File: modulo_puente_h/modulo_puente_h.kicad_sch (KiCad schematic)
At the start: 15 parts, among them M1 Motor_IZQ, M2 Motor_DER, U1 L298N

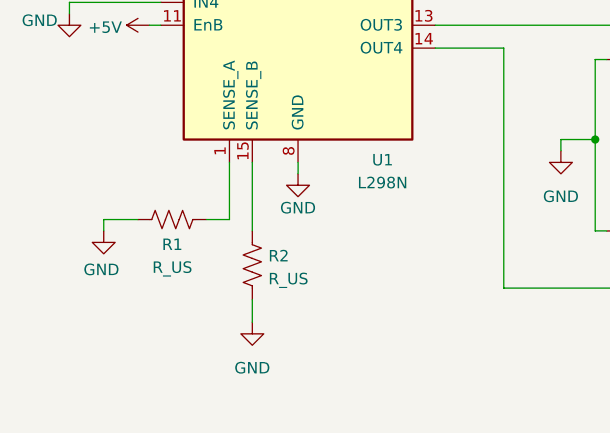
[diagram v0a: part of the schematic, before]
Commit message: fix(puente-h): Las salidas de sensor no tenian PWR_FLAG
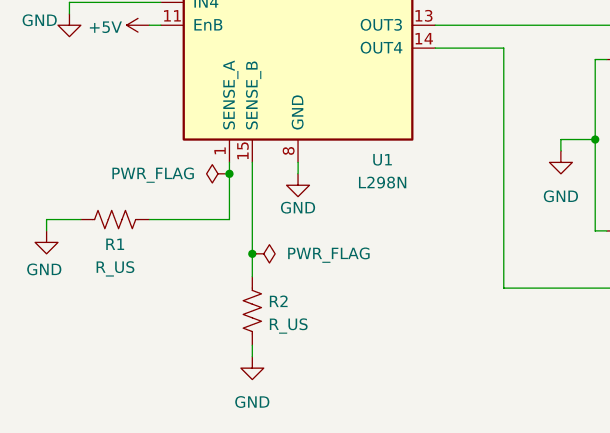
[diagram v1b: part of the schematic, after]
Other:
- moved on the sheet: R1, R2
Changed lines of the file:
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@@
 	)
 	(junction
+		(at 86.36 109.22)
+		(diameter 0)
+		(color 0 0 0 0)
+	)
+	(junction
 		(at 96.52 63.5)
 		(diameter 0)
@@
 	)
 	(junction
+		(at 88.9 118.11)
+		(diameter 0)
+		(color 0 0 0 0)
+	)
+	(junction
 		(at 127 71.12)
 		(diameter 0)
@@
 	(wire
 		(pts
-			(xy 86.36 107.95) (xy 86.36 114.3)
+			(xy 86.36 107.95) (xy 86.36 109.22)
 		)
 		(stroke
@@
 	(wire
 		(pts
-			(xy 86.36 114.3) (xy 83.82 114.3)
+			(xy 86.36 114.3) (xy 77.47 114.3)
 		)
 		(stroke
@@
 	(wire
 		(pts
-			(xy 88.9 125.73) (xy 88.9 123.19)
+			(xy 88.9 129.54) (xy 88.9 128.27)
 		)
 		(stroke
@@
 	(wire
 		(pts
-			(xy 76.2 114.3) (xy 72.39 114.3)
+			(xy 69.85 114.3) (xy 66.04 114.3)
 		)
 		(stroke
@@
 	(wire
 		(pts
-			(xy 88.9 107.95) (xy 88.9 115.57)
+			(xy 88.9 107.95) (xy 88.9 118.11)
 		)
 		(stroke
@@
 	(wire
 		(pts
+			(xy 86.36 109.22) (xy 86.36 114.3)
+		)
+		(stroke
+			(width 0)
+			(type default)
+		)
+	)
+	(wire
+		(pts
 			(xy 205.74 77.47) (xy 209.55 77.47)
 		)
@@
 	(wire
 		(pts
+			(xy 88.9 118.11) (xy 88.9 120.65)
+		)
+		(stroke
+			(width 0)
+			(type default)
+		)
+	)
+	(wire
+		(pts
 			(xy 149.86 115.57) (xy 151.13 115.57)
 		)
@@
 	(wire
 		(pts
-			(xy 72.39 114.3) (xy 72.39 115.57)
+			(xy 66.04 114.3) (xy 66.04 115.57)
 		)
 		(stroke
@@
 	(symbol
 		(lib_id "power:GNDS")
-		(at 72.39 115.57 0)
+		(at 66.04 115.57 0)
 		(unit 1)
 		(exclude_from_sim no)
@@
 		(dnp no)
 		(property "Reference" "#PWR015"
-			(at 72.39 121.92 0)
+			(at 66.04 121.92 0)
 			(effects
 				(font
@@
 		)
 		(property "Value" "GND"
-			(at 72.136 119.888 0)
+			(at 65.786 119.888 0)
 			(effects
 				(font
@@
 		)
 		(property "Footprint" ""
-			(at 72.39 115.57 0)
+			(at 66.04 115.57 0)
 			(effects
 				(font
@@
 		)
 		(property "Datasheet" ""
-			(at 72.39 115.57 0)
+			(at 66.04 115.57 0)
 			(effects
 				(font
@@
 		)
 		(property "Description" "Power symbol creates a global label with name \"GNDS\" , signal ground"
-			(at 72.39 115.57 0)
+			(at 66.04 115.57 0)
 			(effects
 				(font
@@
 	(symbol
 		(lib_id "power:PWR_FLAG")
+		(at 88.9 118.11 270)
+		(unit 1)
+		(exclude_from_sim no)
+		(in_bom yes)
+		(on_board yes)
+		(dnp no)
+		(fields_autoplaced yes)
+		(property "Reference" "#FLG07"
+			(at 90.805 118.11 0)
+			(effects
+				(font
+					(size 1.27 1.27)
+				)
+				(hide yes)
+			)
+		)
+		(property "Value" "PWR_FLAG"
+			(at 92.71 118.1099 90)
+			(effects
+				(font
+					(size 1.27 1.27)
+				)
+				(justify left)
+			)
+		)
+		(property "Footprint" ""
+			(at 88.9 118.11 0)
+			(effects
+				(font
+					(size 1.27 1.27)
+				)
+				(hide yes)
+			)
+		)
+		(property "Datasheet" "~"
+			(at 88.9 118.11 0)
+			(effects
+				(font
+					(size 1.27 1.27)
+				)
+				(hide yes)
+			)
+		)
+		(property "Description" "Special symbol for telling ERC where power comes from"
+			(at 88.9 118.11 0)
+			(effects
+				(font
+					(size 1.27 1.27)
+				)
+				(hide yes)
+			)
+		)
+		(pin "1"
+		)
+		(instances
+			(project "modulo_puente_h"
+				(path "/e8bedf4c-52de-4280-a6f9-25032b7792a2"
+					(reference "#FLG07")
+					(unit 1)
+				)
+			)
+		)
+	)
+	(symbol
+		(lib_id "power:PWR_FLAG")
 		(at 243.84 97.79 0)
 		(unit 1)
@@
 	(symbol
 		(lib_id "power:GNDS")
-		(at 88.9 125.73 0)
+		(at 88.9 129.54 0)
 		(unit 1)
 		(exclude_from_sim no)
@@
 		(fields_autoplaced yes)
 		(property "Reference" "#PWR016"
-			(at 88.9 132.08 0)
+			(at 88.9 135.89 0)
 			(effects
 				(font
@@
 		)
 		(property "Value" "GND"
-			(at 88.9 130.81 0)
+			(at 88.9 134.62 0)
 			(effects
 				(font
@@
 		)
 		(property "Footprint" ""
-			(at 88.9 125.73 0)
+			(at 88.9 129.54 0)
 			(effects
 				(font
@@
 		)
 		(property "Datasheet" ""
-			(at 88.9 125.73 0)
+			(at 88.9 129.54 0)
 			(effects
 				(font
@@
 		)
 		(property "Description" "Power symbol creates a global label with name \"GNDS\" , signal ground"
-			(at 88.9 125.73 0)
+			(at 88.9 129.54 0)
 			(effects
 				(font
@@
 	(symbol
 		(lib_id "Device:R_US")
-		(at 88.9 119.38 180)
+		(at 88.9 124.46 180)
 		(unit 1)
 		(exclude_from_sim no)
@@
 		(dnp no)
 		(property "Reference" "R2"
-			(at 90.678 118.364 0)
+			(at 90.678 123.444 0)
 			(effects
 				(font
@@
 		)
 		(property "Value" "R_US"
-			(at 90.678 120.904 0)
+			(at 90.678 125.984 0)
 			(effects
 				(font
@@
 		)
 		(property "Footprint" ""
-			(at 87.884 119.126 90)
+			(at 87.884 124.206 90)
 			(effects
 				(font
@@
 		)
 		(property "Datasheet" "~"
-			(at 88.9 119.38 0)
+			(at 88.9 124.46 0)
 			(effects
 				(font
@@
 		)
 		(property "Description" "Resistor, US symbol"
-			(at 88.9 119.38 0)
+			(at 88.9 124.46 0)
 			(effects
 				(font
@@
 	)
 	(symbol
+		(lib_id "power:PWR_FLAG")
+		(at 86.36 109.22 90)
+		(unit 1)
+		(exclude_from_sim no)
+		(in_bom yes)
+		(on_board yes)
+		(dnp no)
+		(fields_autoplaced yes)
+		(property "Reference" "#FLG06"
+			(at 84.455 109.22 0)
+			(effects
+				(font
+					(size 1.27 1.27)
+				)
+				(hide yes)
+			)
+		)
+		(property "Value" "PWR_FLAG"
+			(at 82.55 109.2199 90)
+			(effects
+				(font
+					(size 1.27 1.27)
+				)
+				(justify left)
+			)
+		)
+		(property "Footprint" ""
+			(at 86.36 109.22 0)
+			(effects
+				(font
+					(size 1.27 1.27)
+				)
+				(hide yes)
+			)
+		)
+		(property "Datasheet" "~"
+			(at 86.36 109.22 0)
+			(effects
+				(font
+					(size 1.27 1.27)
+				)
+				(hide yes)
+			)
+		)
+		(property "Description" "Special symbol for telling ERC where power comes from"
+			(at 86.36 109.22 0)
+			(effects
+				(font
+					(size 1.27 1.27)
+				)
+				(hide yes)
+			)
+		)
+		(pin "1"
+		)
+		(instances
+			(project ""
+				(path "/e8bedf4c-52de-4280-a6f9-25032b7792a2"
+					(reference "#FLG06")
+					(unit 1)
+				)
+			)
+		)
+	)
+	(symbol
 		(lib_id "power:GND")
 		(at 123.19 106.68 0)
@@
 	(symbol
 		(lib_id "Device:R_US")
-		(at 80.01 114.3 270)
+		(at 73.66 114.3 270)
 		(unit 1)
 		(exclude_from_sim no)
@@
 		(dnp no)
 		(property "Reference" "R1"
-			(at 80.01 117.094 90)
+			(at 73.66 117.094 90)
 			(effects
 				(font
@@
 		)
 		(property "Value" "R_US"
-			(at 80.01 119.634 90)
+			(at 73.66 119.634 90)
 			(effects
 				(font
@@
 		)
 		(property "Footprint" ""
-			(at 79.756 115.316 90)
+			(at 73.406 115.316 90)
 			(effects
 				(font
@@
 		)
 		(property "Datasheet" "~"
-			(at 80.01 114.3 0)
+			(at 73.66 114.3 0)
 			(effects
 				(font
@@
 		)
 		(property "Description" "Resistor, US symbol"
-			(at 80.01 114.3 0)
+			(at 73.66 114.3 0)
 			(effects
 				(font

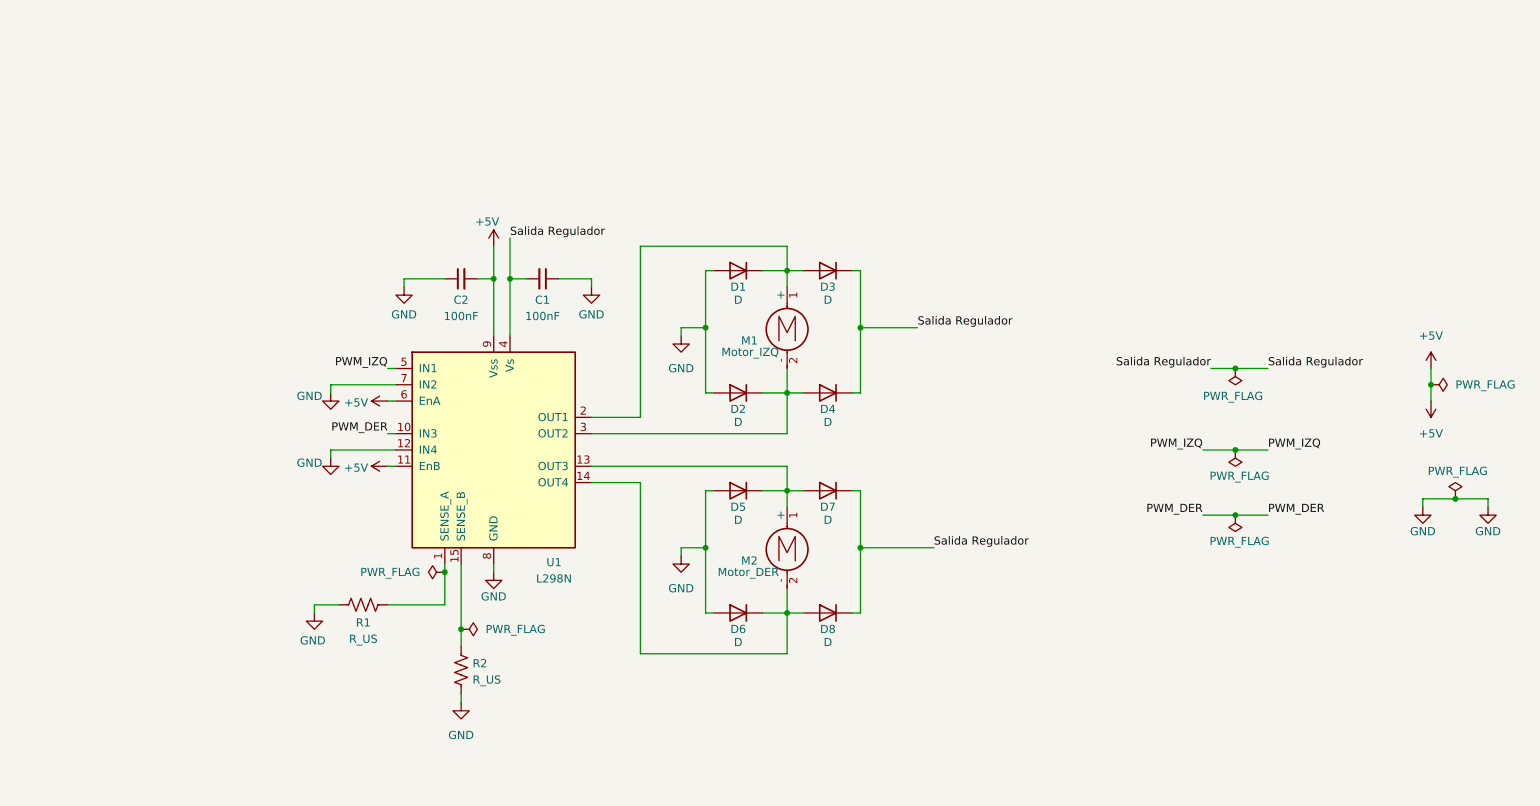
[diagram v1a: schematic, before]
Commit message: refactor(puente-h):Modifico el orden de los pines de conexión
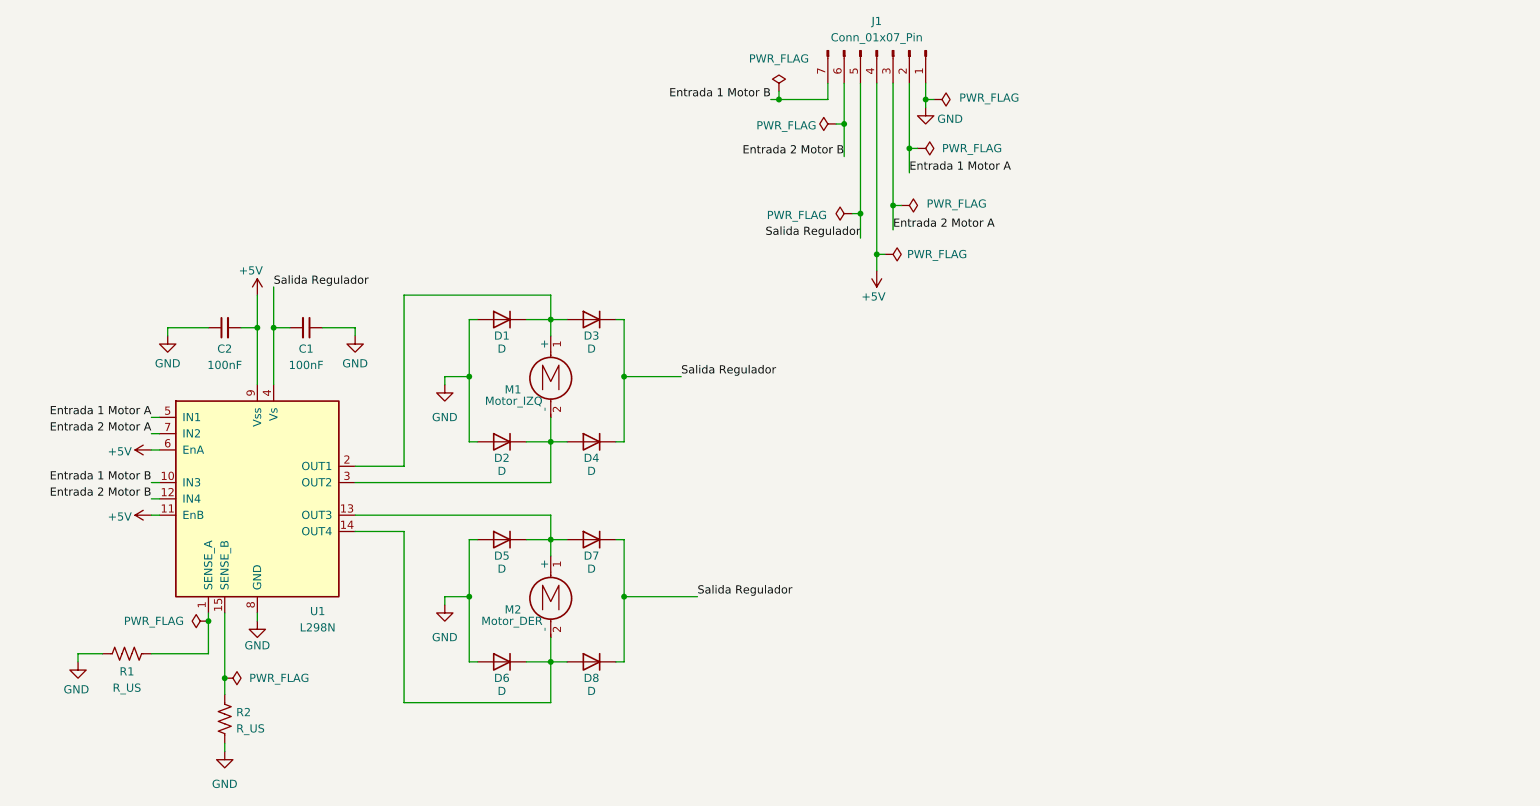
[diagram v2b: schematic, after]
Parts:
- added J1: Conn_01x07_Pin, Connector_PinHeader_2.54mm:PinHeader_1x07_P2.54mm_Vertical, symbol Connector:Conn_01x07_Pin
- C1, C2: footprint (none) -> Capacitor_THT:C_Disc_D7.0mm_W2.5mm_P5.00mm
- D1, D2, D3, D4, D5, D6, D7, D8: footprint (none) -> Diode_THT:D_DO-41_SOD81_P7.62mm_Horizontal
- M1, M2: footprint (none) -> Resistor_THT:R_Axial_DIN0207_L6.3mm_D2.5mm_P2.54mm_Vertical
- R1, R2: footprint (none) -> Resistor_SMD:R_0805_2012Metric_Pad1.20x1.40mm_HandSolder
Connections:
- net +5V: now also J1.4 (Pin_4)
- net GND: now also J1.1 (Pin_1); no longer U1.12 (IN4), U1.7 (IN2)
- net Salida Regulador: now also J1.5 (Pin_5)
- net PWM_DER renamed Entrada 1 Motor B
- net Entrada 1 Motor B: now also J1.7 (Pin_7)
- net PWM_IZQ renamed Entrada 1 Motor A
- net Entrada 1 Motor A: now also J1.2 (Pin_2)
- new net Entrada 2 Motor A: J1.3 (Pin_3), U1.7 (IN2)
- new net Entrada 2 Motor B: J1.6 (Pin_6), U1.12 (IN4)
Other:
- moved on the sheet: C1, C2, D1, D2, D3, D4, D5, D6, D7, D8, M1, M2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
